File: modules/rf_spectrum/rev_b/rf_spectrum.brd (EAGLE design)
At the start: 68.1 x 66 mm, 44 parts, among them J3 MODULE_GENERIC_DEBUGSMT, J4 TC2030-JLINK-L, Q1 SI223DDS, U1 MWSUB3G, U2 SKY13317, U3 STM32L432KC, U4 TLV62130, X1 ABS05-32.768KHZ-T

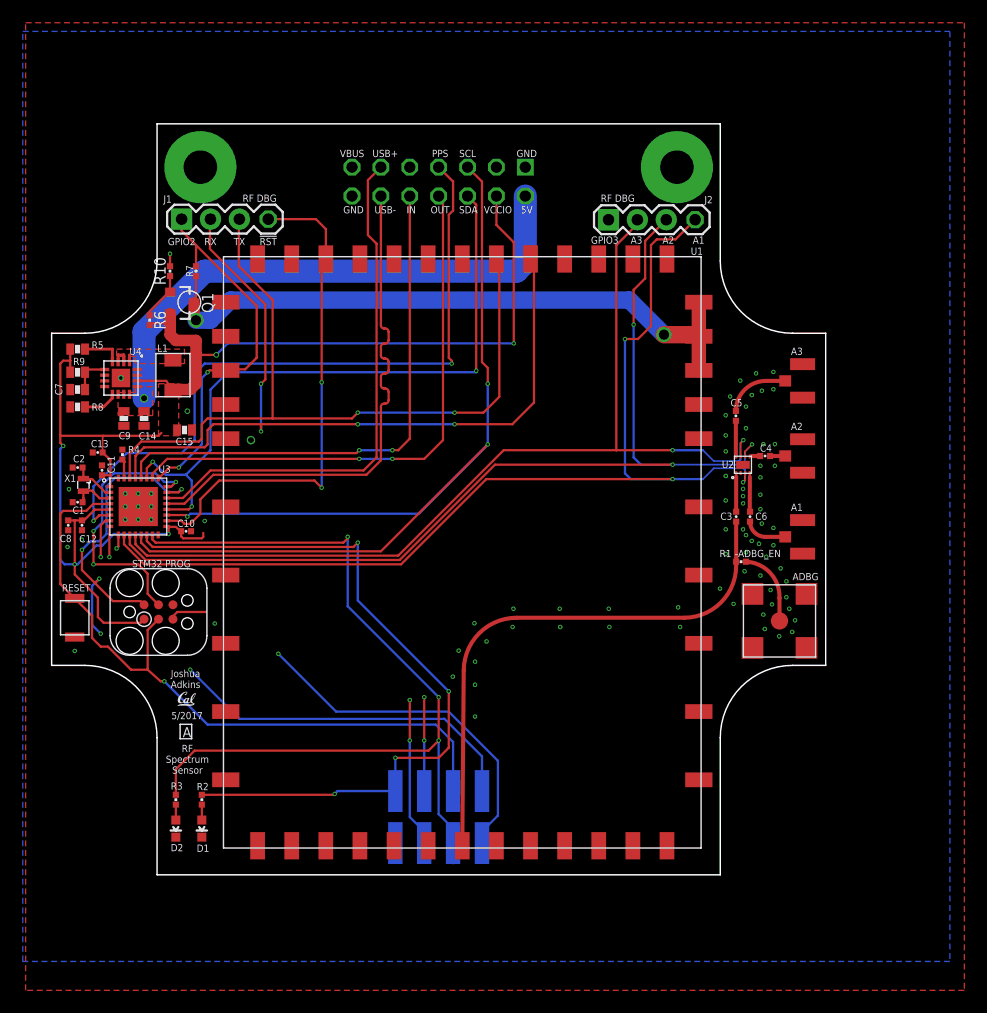
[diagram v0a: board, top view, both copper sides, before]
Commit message: added rf spectrum cleanups, especially to BOM
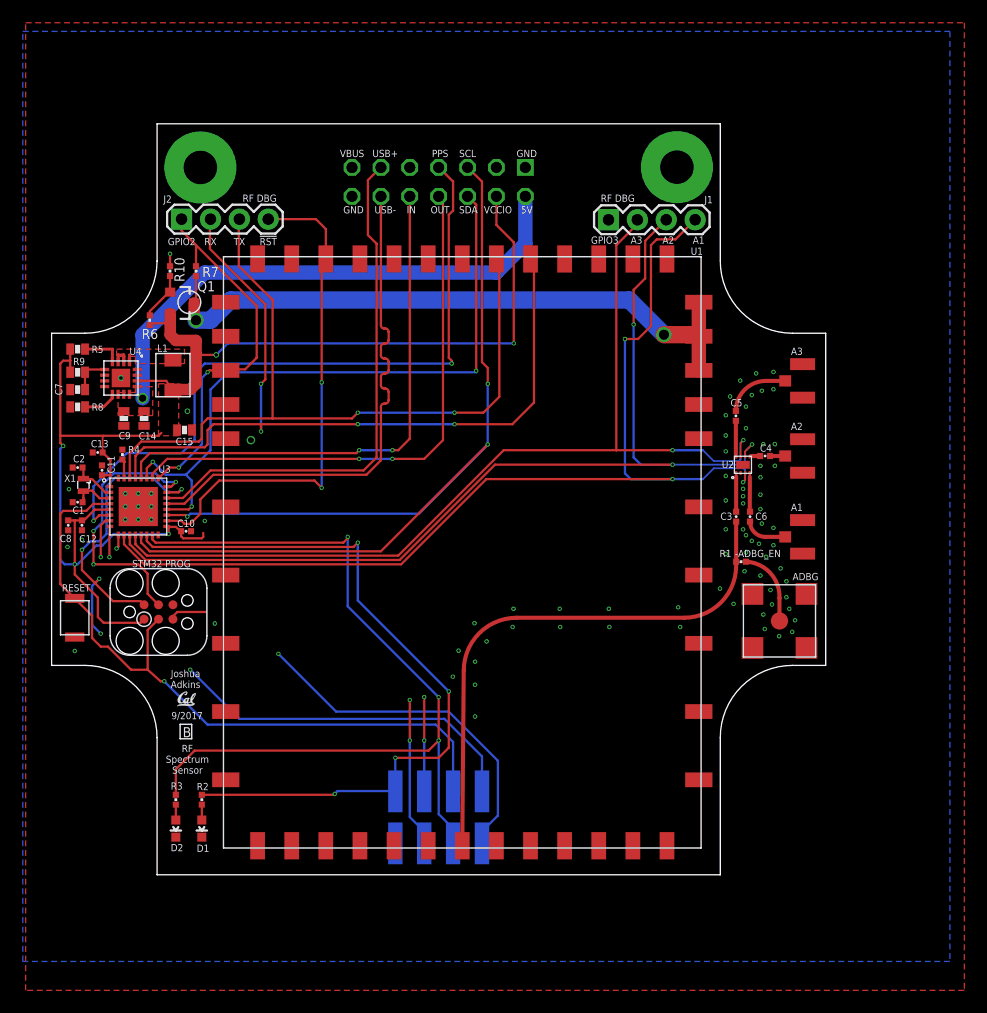
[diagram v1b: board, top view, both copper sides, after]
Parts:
- added J5: TC2030-JLINK-L, connector:TC2030-IDC
- J3: value MODULE_GENERIC_DEBUGSMT -> SIGNPOST_DEBUG_HEADERSMT; device signpost:MODULE_GENERIC_DEBUG_SMT -> signpost:SIGNPOST_DEBUG_HEADER_SMT
- J4: value TC2030-JLINK-L -> SIGNPOST_MODULE_HEADER; device connector:TC2030-IDC -> signpost:SIGNPOST_MODULE_HEADER
- R1: value 0 -> DNP - 0
- moved J4 45.1 mm to (36.6, 63.5)
- moved J1 37.5 mm to (51.5, 60.1)
- moved J2 37.5 mm to (14.0, 60.2)
- moved J3 27.9 mm to (36.6, 7.65)
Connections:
- net !RF_RESET: now also J2.4; no longer J1.4
- net !RST: now also J5.3; no longer J4.3
- net 3V3: now also J4.4, J5.1; no longer J3.4, J4.1
- net 5V: now also J4.2; no longer J3.2
- net GND: now also J4.1, J4.14, J5.5, U2.PAD; no longer J3.1, J3.14, J4.5, U2.P$1
- net MOD_IN: now also J4.10; no longer J3.10
- net MOD_OUT: now also J4.8; no longer J3.8
- net PPS: now also J4.7; no longer J3.7
- net RF_ANT1: now also J1.4; no longer J2.4
- net RF_ANT2: now also J1.3; no longer J2.3
- net RF_ANT3: now also J1.2; no longer J2.2
- net RF_GPIO2: now also J2.1; no longer J1.1
- net RF_GPIO3: now also J1.1; no longer J2.1
- net RF_RX: now also J2.2; no longer J1.2
- net RF_TX: now also J2.3; no longer J1.3
- net SCL: now also J4.5; no longer J3.5
- net SDA: now also J4.6; no longer J3.6
- net SWDCLK: now also J5.4; no longer J4.4
- net SWDIO: now also J5.2; no longer J4.2
- net USB+: now also J4.11; no longer J3.11
- net USB-: now also J4.12; no longer J3.12
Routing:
- net DBG_GPIO2: track 76.9 -> 75.2 mm
- net 5V: track 48.0 -> 47.0 mm
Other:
- board text added: "0.1 / 2.54 Above PCB"
- board text added: "0.358 / 9.10 Below PCB"
- board text added: "9/2017"
- board text added: "B"
- board text added: "Drill 0.116 @ (-0.825, -1.15)"
- board text added: "Drill 0.116 @ (-0.825, 1.15)"
- board text added: "Drill 0.116 @ (0.825, -1.15)"
- board text added: "Drill 0.116 @ (0.825, 1.15)"
- board text removed: "5/2017"
- board text removed: "A"

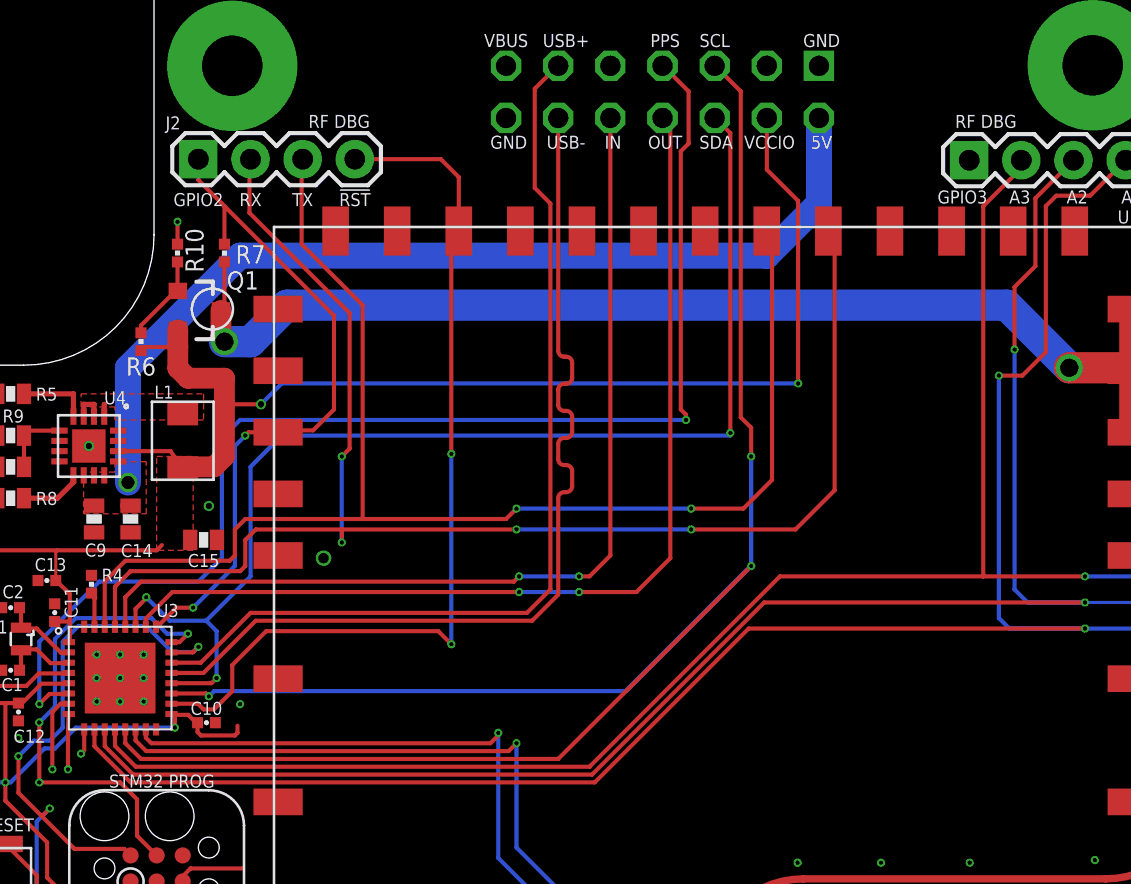
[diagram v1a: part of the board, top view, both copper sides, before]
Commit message: fixed pin mapping, added RTS/CTS
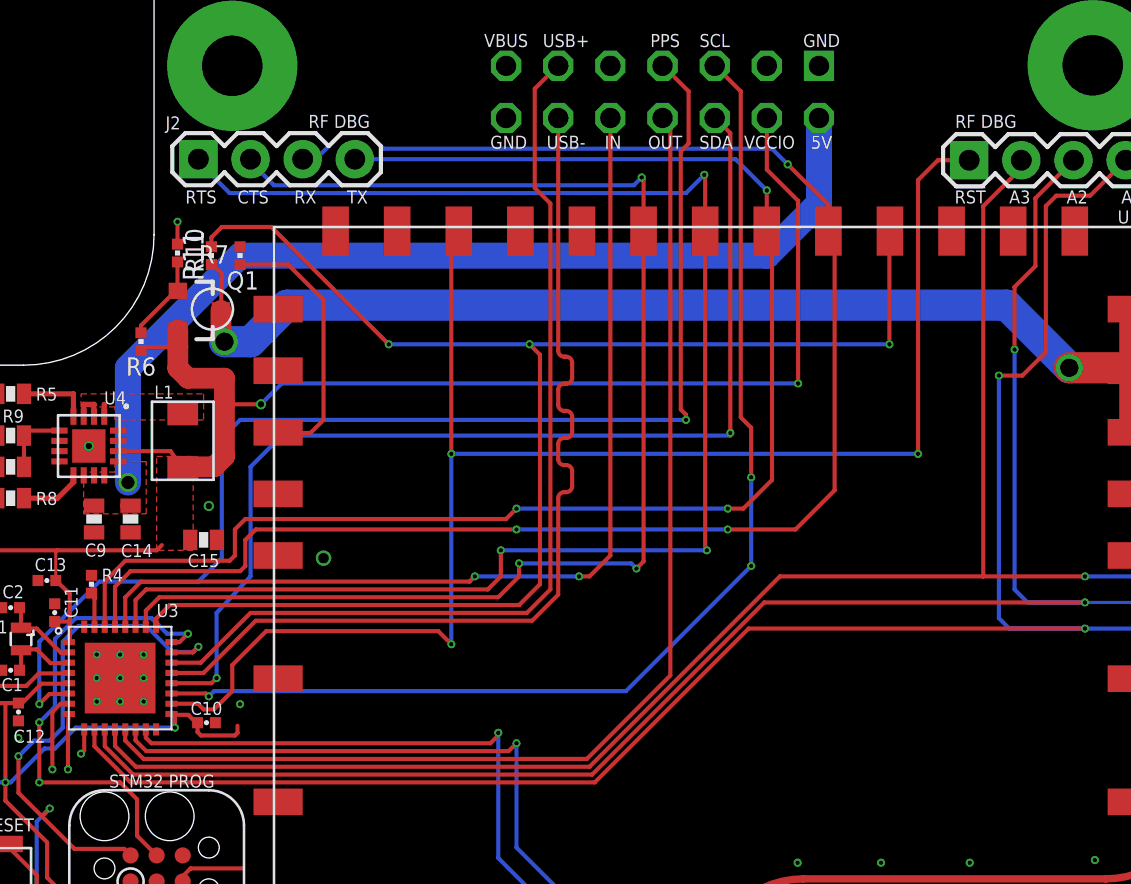
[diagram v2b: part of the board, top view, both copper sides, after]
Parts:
- added R11: 100k, passives:0402_RES
- moved R7 0.77 mm to (16.0, 55.5), turned to 90 degrees
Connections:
- new net RF_CTS/GPIO1: J2.2, U1.41, U3.26
- new net RF_RTS/GPIO0: J2.1, U1.40, U3.27
- net !RF_RESET: now also J1.1; no longer J2.4
- net GATED: now also R11.1; no longer R7.2
- net GND: now also R7.2
- net MOD_OUT: now also U3.13; no longer U3.26
- net RF_GPIO2: no longer J2.1, U3.25
- net RF_GPIO3: now also R11.2, U1.37, U3.25; no longer J1.1
- net RF_RX: now also J2.3; no longer J2.2
- net RF_TX: now also J2.4; no longer J2.3
- net SCL: no longer U3.13
- net SDA: no longer U3.27
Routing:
- net RF_RTS/GPIO0: track 0.00 -> 75.0 mm, vias 0 -> 3
- net RF_GPIO3: track 0.07 -> 73.3 mm, vias 0 -> 3
- net RF_CTS/GPIO1: track 0.00 -> 65.2 mm, vias 0 -> 3
- net SCL: track 100.2 -> 56.0 mm
- net !RF_RESET: track 44.6 -> 75.6 mm, vias 2 -> 3
- net RF_GPIO2: track 33.2 -> 13.2 mm, vias 2 -> 0
- net MOD_OUT: track 48.8 -> 56.5 mm, vias 2 -> 0
- net RF_RX: track 74.0 -> 81.3 mm, vias 4 -> 3
- net SDA: track 58.5 -> 53.0 mm, vias 3 -> 2
- net RF_TX: track 68.6 -> 72.5 mm, vias 2 -> 3
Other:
- board text added: "CTS"
- board text added: "RTS"
- board text removed: "GPIO2"
- board text removed: "GPIO3"
